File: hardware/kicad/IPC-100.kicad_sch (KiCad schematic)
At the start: 0 parts

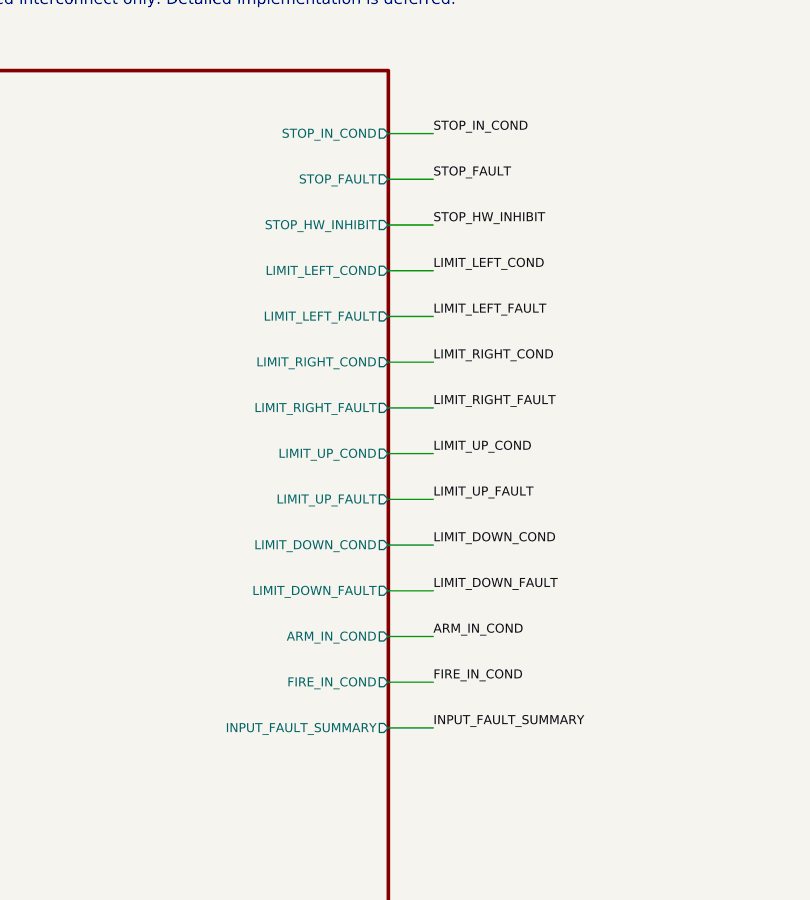
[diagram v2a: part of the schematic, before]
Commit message: Implement supervised safety input subsystem
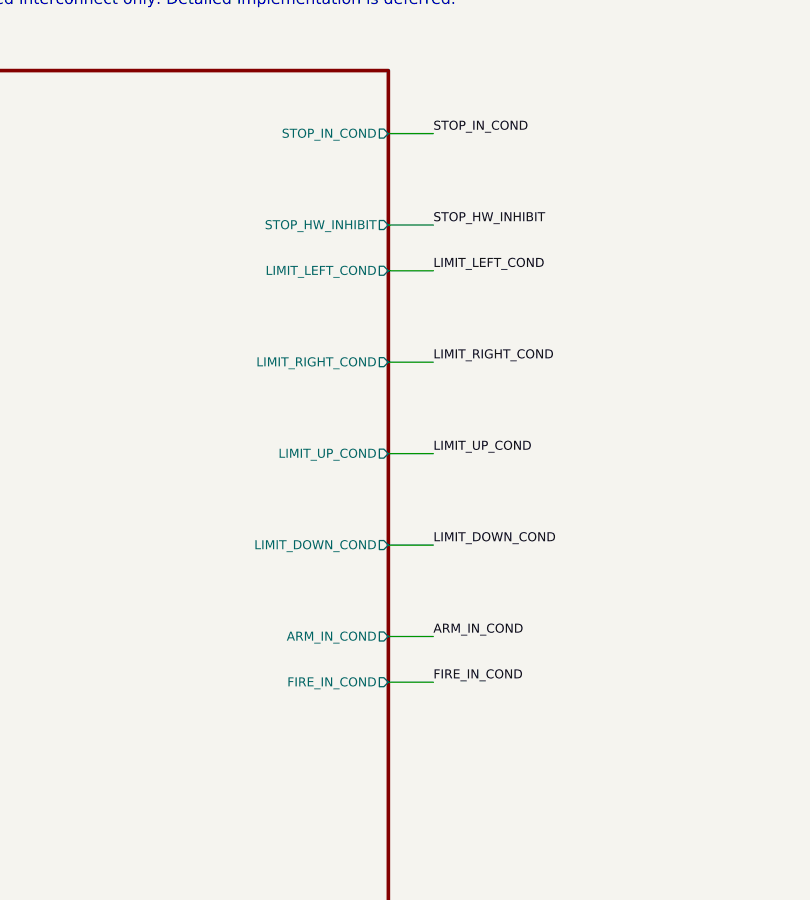
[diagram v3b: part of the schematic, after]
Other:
- sheet 04 Safety Inputs ports: added none; removed INPUT_FAULT_SUMMARY, LIMIT_DOWN_FAULT, LIMIT_LEFT_FAULT, LIMIT_RIGHT_FAULT, LIMIT_UP_FAULT, STOP_FAULT
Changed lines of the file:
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@@
-      (effects (font (size 1.0 1.0)) (justify right))
-    )
-    (pin "STOP_FAULT" output (at 110 37.08 0)
       (effects (font (size 1.0 1.0)) (justify right))
     )
@@
       (effects (font (size 1.0 1.0)) (justify right))
     )
-    (pin "LIMIT_LEFT_FAULT" output (at 110 52.32 0)
-      (effects (font (size 1.0 1.0)) (justify right))
-    )
     (pin "LIMIT_RIGHT_COND" output (at 110 57.40 0)
-      (effects (font (size 1.0 1.0)) (justify right))
-    )
-    (pin "LIMIT_RIGHT_FAULT" output (at 110 62.48 0)
       (effects (font (size 1.0 1.0)) (justify right))
     )
@@
       (effects (font (size 1.0 1.0)) (justify right))
     )
-    (pin "LIMIT_UP_FAULT" output (at 110 72.64 0)
-      (effects (font (size 1.0 1.0)) (justify right))
-    )
     (pin "LIMIT_DOWN_COND" output (at 110 77.72 0)
-      (effects (font (size 1.0 1.0)) (justify right))
-    )
-    (pin "LIMIT_DOWN_FAULT" output (at 110 82.80 0)
       (effects (font (size 1.0 1.0)) (justify right))
     )
@@
     )
     (pin "FIRE_IN_COND" output (at 110 92.96 0)
-      (effects (font (size 1.0 1.0)) (justify right))
-    )
-    (pin "INPUT_FAULT_SUMMARY" output (at 110 98.04 0)
       (effects (font (size 1.0 1.0)) (justify right))
     )
@@
     (effects (font (size 1.0 1.0)) (justify left bottom))
   )
-  (wire (pts (xy 110 37.08) (xy 115 37.08))
-    (stroke (width 0) (type default))
-  )
-  (label "STOP_FAULT" (at 115 37.08 0)
-    (effects (font (size 1.0 1.0)) (justify left bottom))
-  )
   (wire (pts (xy 110 42.16) (xy 115 42.16))
     (stroke (width 0) (type default))
@@
     (effects (font (size 1.0 1.0)) (justify left bottom))
   )
-  (wire (pts (xy 110 52.32) (xy 115 52.32))
-    (stroke (width 0) (type default))
-  )
-  (label "LIMIT_LEFT_FAULT" (at 115 52.32 0)
-    (effects (font (size 1.0 1.0)) (justify left bottom))
-  )
   (wire (pts (xy 110 57.40) (xy 115 57.40))
     (stroke (width 0) (type default))
   )
   (label "LIMIT_RIGHT_COND" (at 115 57.40 0)
-    (effects (font (size 1.0 1.0)) (justify left bottom))
-  )
-  (wire (pts (xy 110 62.48) (xy 115 62.48))
-    (stroke (width 0) (type default))
-  )
-  (label "LIMIT_RIGHT_FAULT" (at 115 62.48 0)
     (effects (font (size 1.0 1.0)) (justify left bottom))
   )
@@
     (effects (font (size 1.0 1.0)) (justify left bottom))
   )
-  (wire (pts (xy 110 72.64) (xy 115 72.64))
-    (stroke (width 0) (type default))
-  )
-  (label "LIMIT_UP_FAULT" (at 115 72.64 0)
-    (effects (font (size 1.0 1.0)) (justify left bottom))
-  )
   (wire (pts (xy 110 77.72) (xy 115 77.72))
     (stroke (width 0) (type default))
   )
   (label "LIMIT_DOWN_COND" (at 115 77.72 0)
-    (effects (font (size 1.0 1.0)) (justify left bottom))
-  )
-  (wire (pts (xy 110 82.80) (xy 115 82.80))
-    (stroke (width 0) (type default))
-  )
-  (label "LIMIT_DOWN_FAULT" (at 115 82.80 0)
     (effects (font (size 1.0 1.0)) (justify left bottom))
   )
@@
     (effects (font (size 1.0 1.0)) (justify left bottom))
   )
-  (wire (pts (xy 110 98.04) (xy 115 98.04))
-    (stroke (width 0) (type default))
-  )
-  (label "INPUT_FAULT_SUMMARY" (at 115 98.04 0)
-    (effects (font (size 1.0 1.0)) (justify left bottom))
-  )

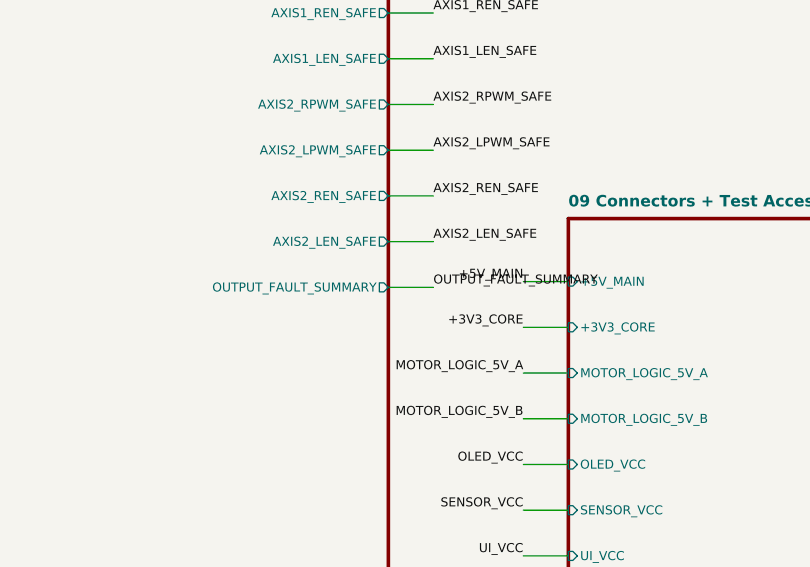
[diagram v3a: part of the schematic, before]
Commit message: Resolve Rev A motion interface contract
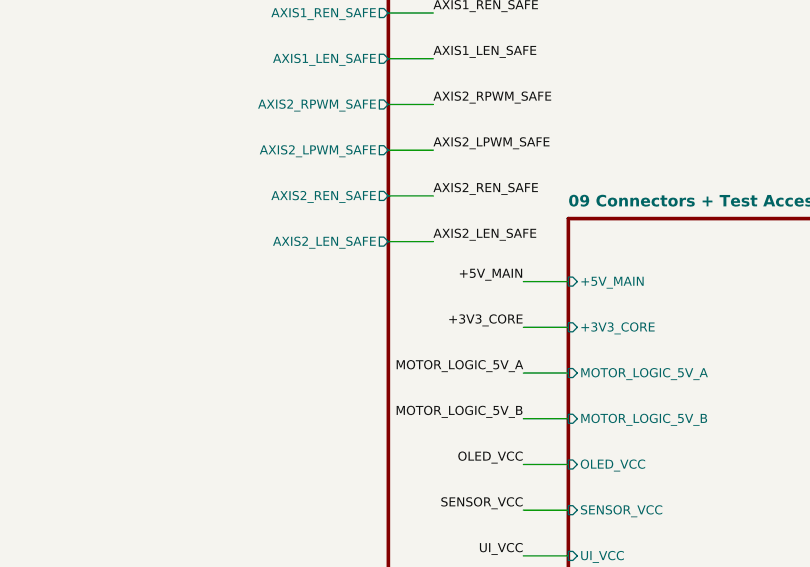
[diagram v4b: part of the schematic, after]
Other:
- sheet 05 Motor Interfaces ports: added none; removed OUTPUT_FAULT_SUMMARY
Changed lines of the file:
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@@
-      (effects (font (size 1.0 1.0)) (justify right))
-    )
-    (pin "OUTPUT_FAULT_SUMMARY" output (at 470 72.64 0)
       (effects (font (size 1.0 1.0)) (justify right))
     )
@@
     (effects (font (size 1.0 1.0)) (justify left bottom))
   )
-  (wire (pts (xy 470 72.64) (xy 475 72.64))
-    (stroke (width 0) (type default))
-  )
-  (label "OUTPUT_FAULT_SUMMARY" (at 475 72.64 0)
-    (effects (font (size 1.0 1.0)) (justify left bottom))
-  )

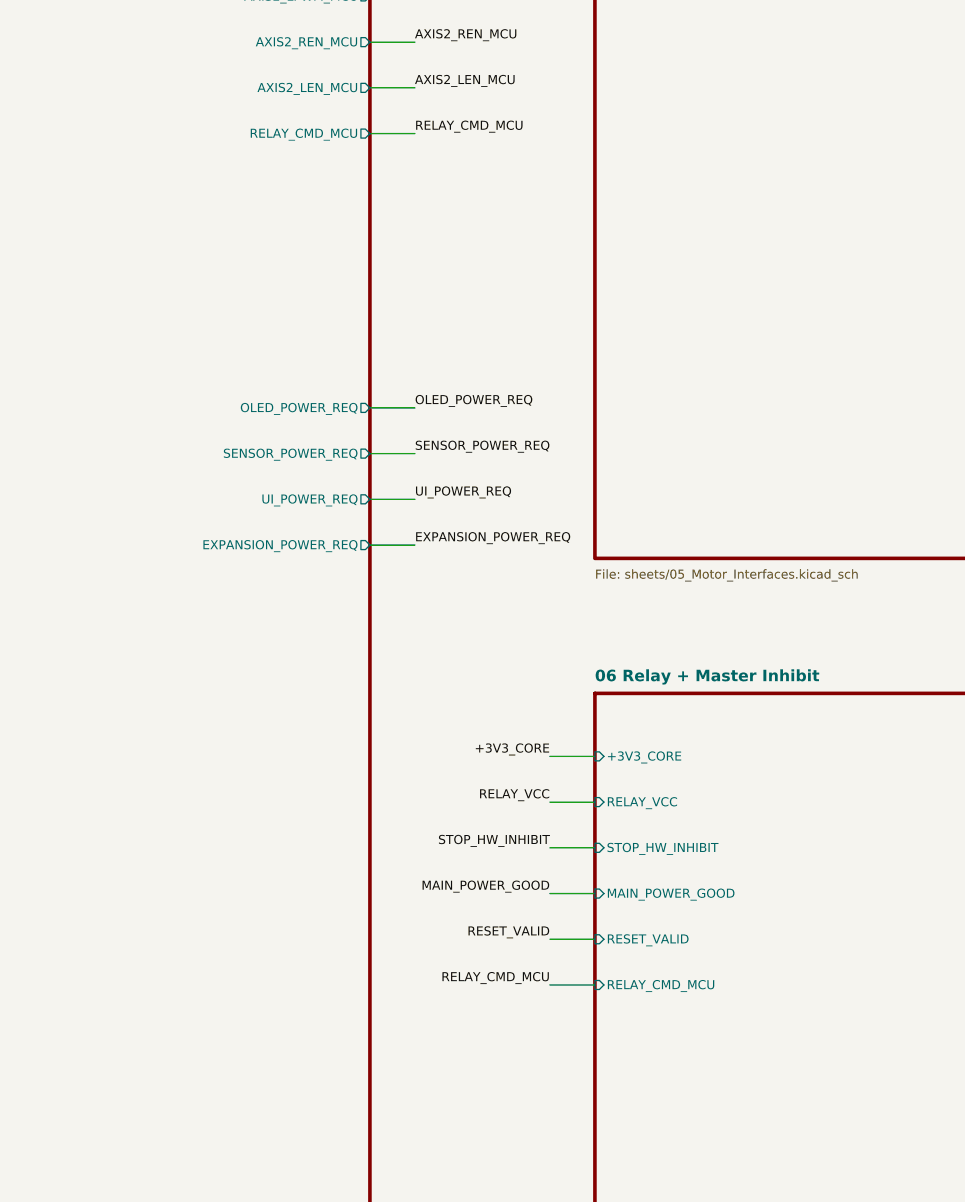
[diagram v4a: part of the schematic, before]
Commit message: Resolve independent watchdog service interface
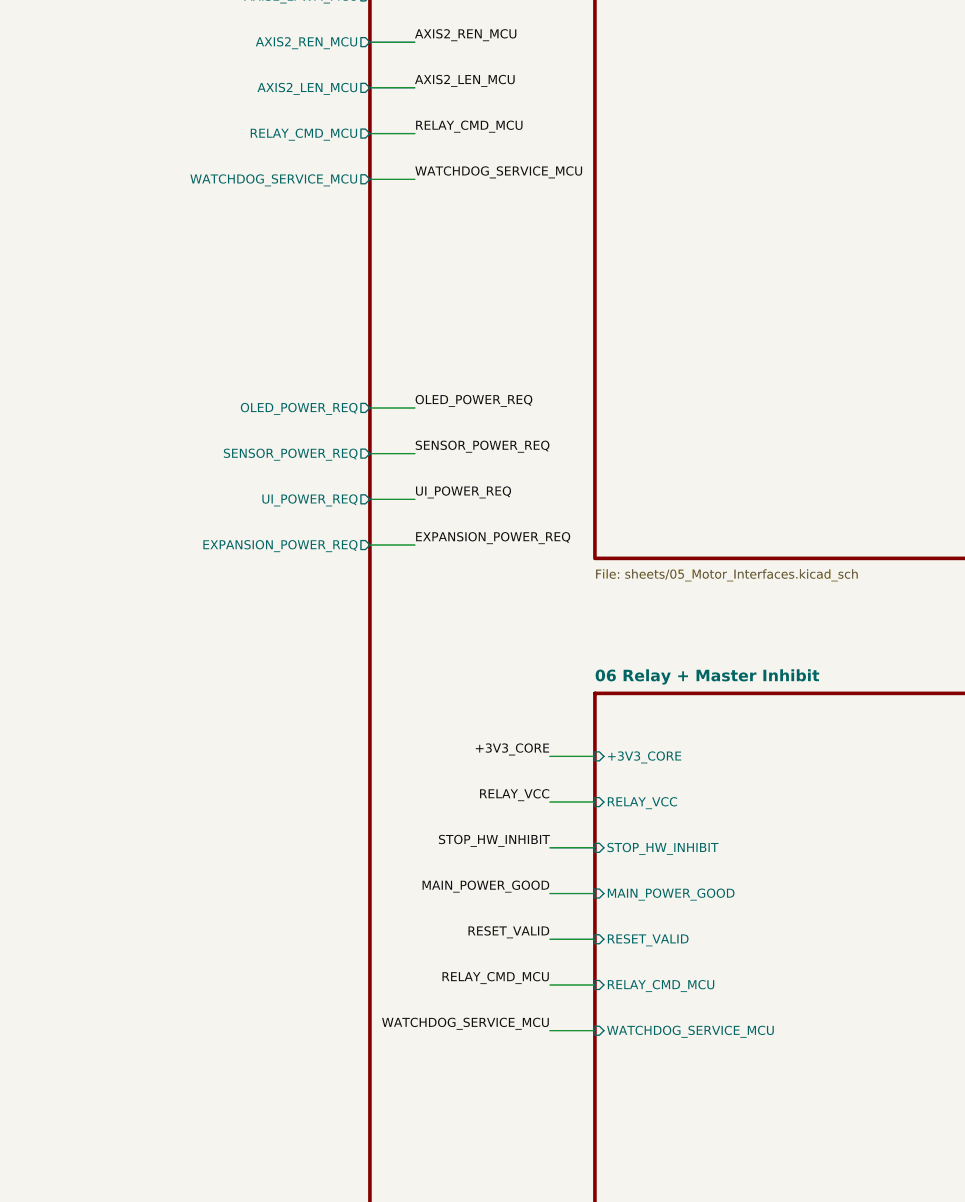
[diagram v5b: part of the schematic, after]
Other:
- sheet 03 ESP32 Core ports: added WATCHDOG_SERVICE_MCU; removed none
- sheet 06 Relay + Master Inhibit ports: added WATCHDOG_SERVICE_MCU; removed none
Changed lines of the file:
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@@
+      (effects (font (size 1.0 1.0)) (justify right))
+    )
+    (pin "WATCHDOG_SERVICE_MCU" output (at 350 137.88 0)
       (effects (font (size 1.0 1.0)) (justify right))
     )
@@
   )
   (label "RELAY_CMD_MCU" (at 355 132.80 0)
+    (effects (font (size 1.0 1.0)) (justify left bottom))
+  )
+  (wire (pts (xy 350 137.88) (xy 355 137.88))
+    (stroke (width 0) (type default))
+  )
+  (label "WATCHDOG_SERVICE_MCU" (at 355 137.88 0)
     (effects (font (size 1.0 1.0)) (justify left bottom))
   )
@@
       (effects (font (size 1.0 1.0)) (justify left))
     )
+    (pin "WATCHDOG_SERVICE_MCU" input (at 375 232.48 180)
+      (effects (font (size 1.0 1.0)) (justify left))
+    )
     (pin "MASTER_INHIBIT" output (at 470 202.00 0)
       (effects (font (size 1.0 1.0)) (justify right))
@@
     (effects (font (size 1.0 1.0)) (justify right bottom))
   )
+  (wire (pts (xy 375 232.48) (xy 370 232.48))
+    (stroke (width 0) (type default))
+  )
+  (label "WATCHDOG_SERVICE_MCU" (at 370 232.48 180)
+    (effects (font (size 1.0 1.0)) (justify right bottom))
+  )
